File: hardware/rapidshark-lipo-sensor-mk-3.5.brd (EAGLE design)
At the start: 30.5 x 17.8 mm, 26 parts, among them Q1 IRLML2244, Q2 IRLML2502, Q3 IRLML2244, Q4 IRLML2502, Q5 IRLML2244, Q6 IRLML2502, U1 Tiny84

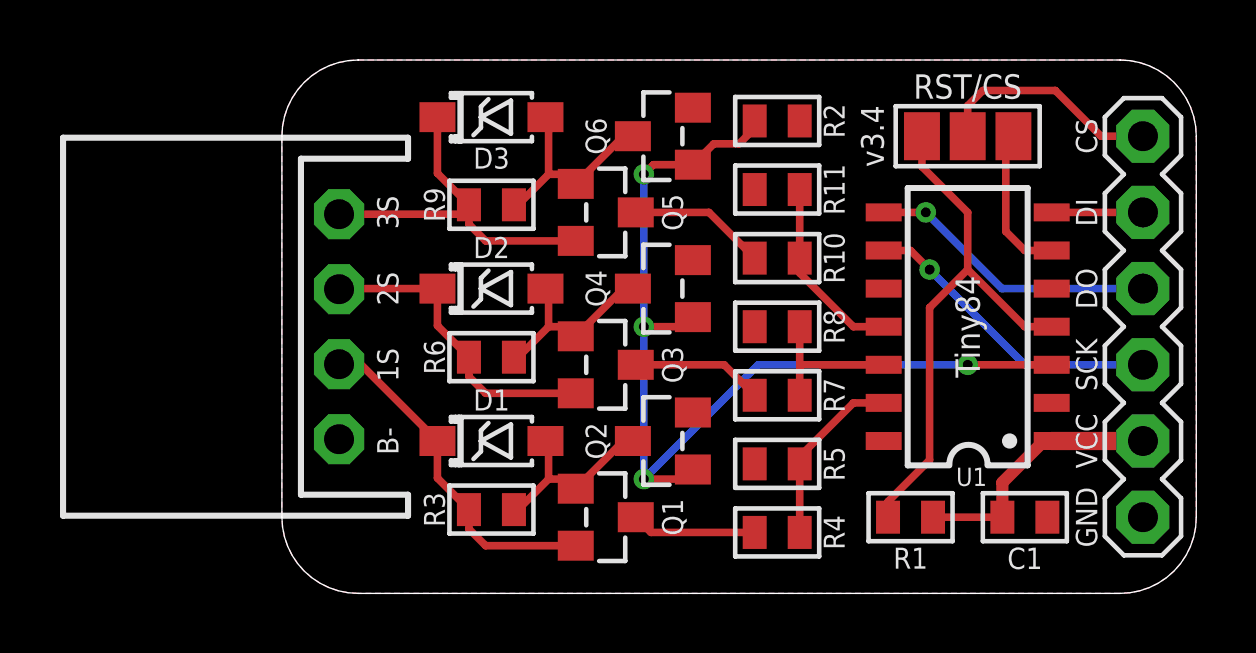
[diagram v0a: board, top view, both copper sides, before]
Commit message: lipo sensors suck
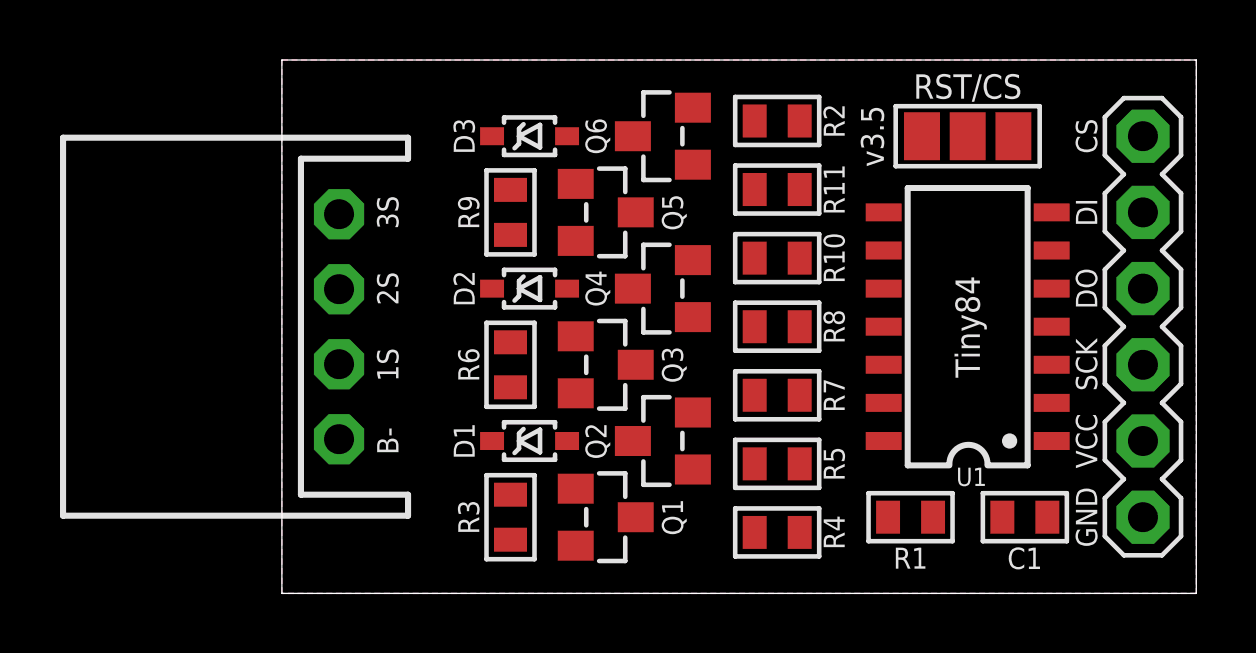
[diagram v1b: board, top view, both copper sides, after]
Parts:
- D1, D2, D3: device a_parts:SOD123-ZENER -> a_parts:SOD323-ZENNER
- Q1, Q3, Q5: value IRLML2244 -> BSH203
- moved D3 1.42 mm to (8.26, 15.2)
- moved D1 1.27 mm to (8.26, 5.08)
- moved D2 1.27 mm to (8.26, 10.2)
- moved R9 0.68 mm to (7.62, 12.7), turned to 90 degrees
- moved R3 0.68 mm to (7.62, 2.54), turned to 90 degrees
- moved R6 0.68 mm to (7.62, 7.62), turned to 90 degrees
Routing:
- net EN_DIV: track 33.4 -> 0.00 mm, vias 4 -> 0
- net RESET: track 18.0 -> 0.00 mm
- net CELL3+: track 12.3 -> 0.00 mm
- net CELL1+: track 11.5 -> 0.00 mm
- net CELL2+: track 10.4 -> 0.00 mm
- net SCK: track 10.2 -> 0.00 mm, vias 1 -> 0
- net DO/MISO: track 9.69 -> 0.00 mm, vias 1 -> 0
- net VCC: track 8.73 -> 0.00 mm
- net RST/CS: track 7.70 -> 0.00 mm
- net N$7: track 7.13 -> 0.00 mm
- net N$5: track 6.49 -> 0.00 mm
- net N$4: track 6.49 -> 0.00 mm
- net VDIV3: track 6.32 -> 0.00 mm
- net VDIV1: track 6.07 -> 0.00 mm
- net VDIV2: track 5.09 -> 0.00 mm
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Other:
- outline, holes or cut-outs redrawn
